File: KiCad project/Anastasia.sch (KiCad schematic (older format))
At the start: 12 parts, among them U1 EFM32GG332

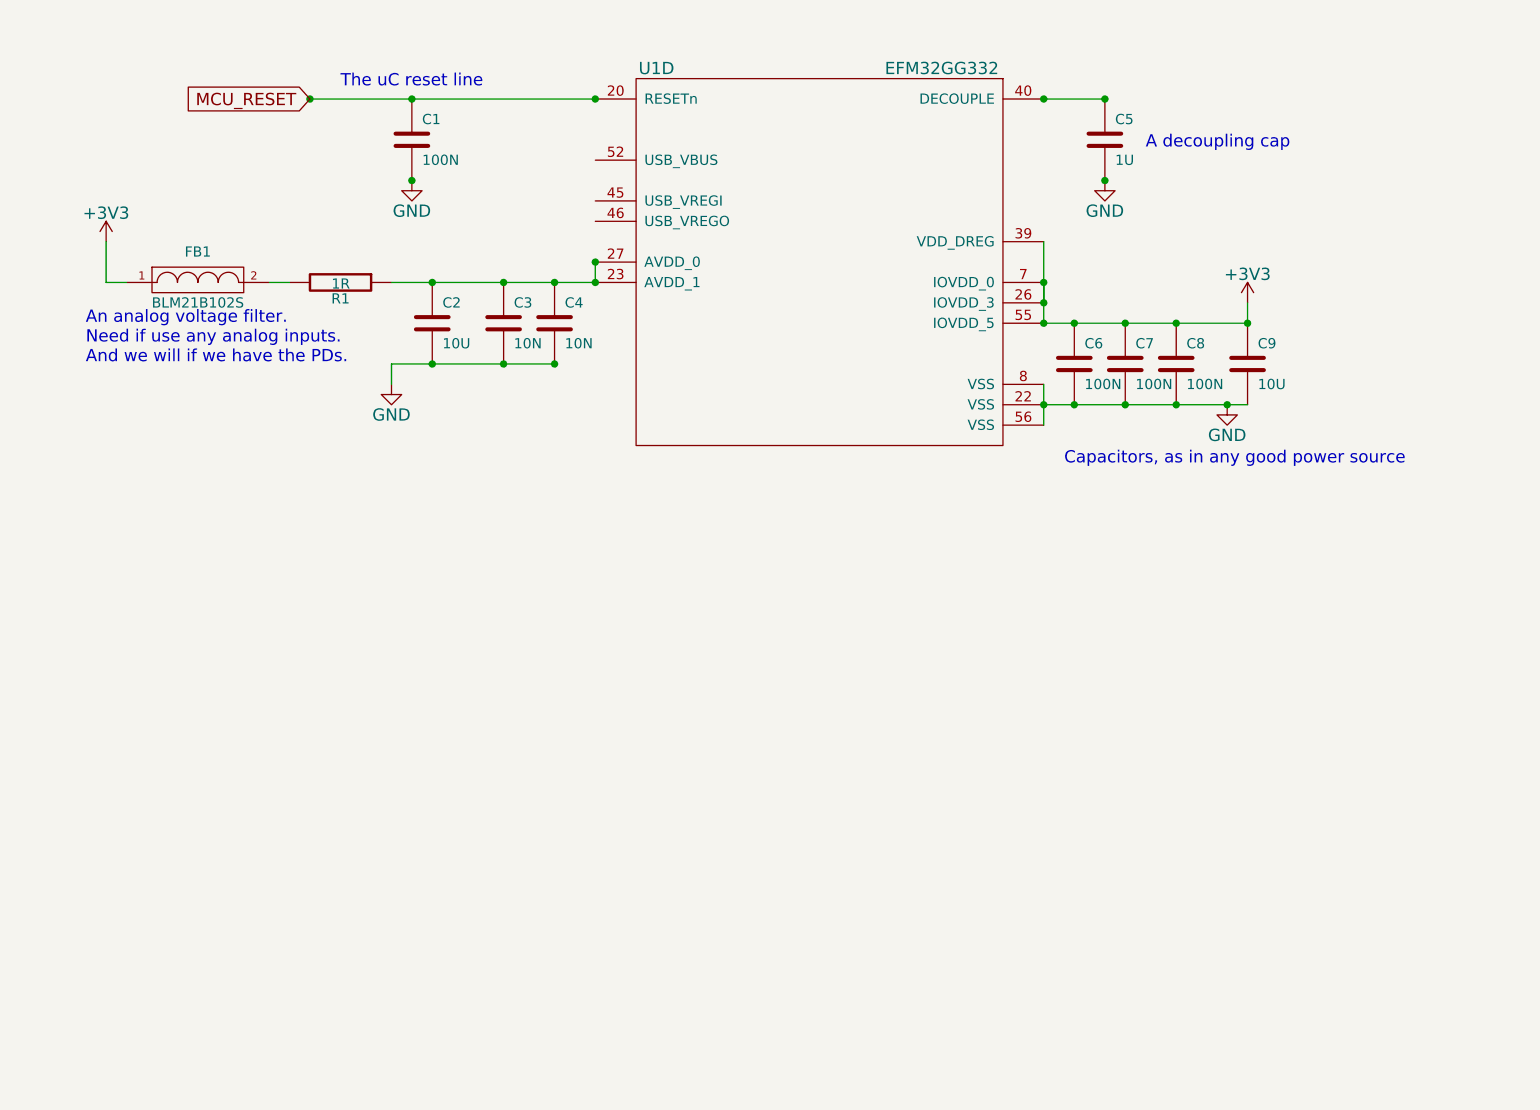
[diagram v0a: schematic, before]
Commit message: Power and USB schematics
The actual schematics file updates
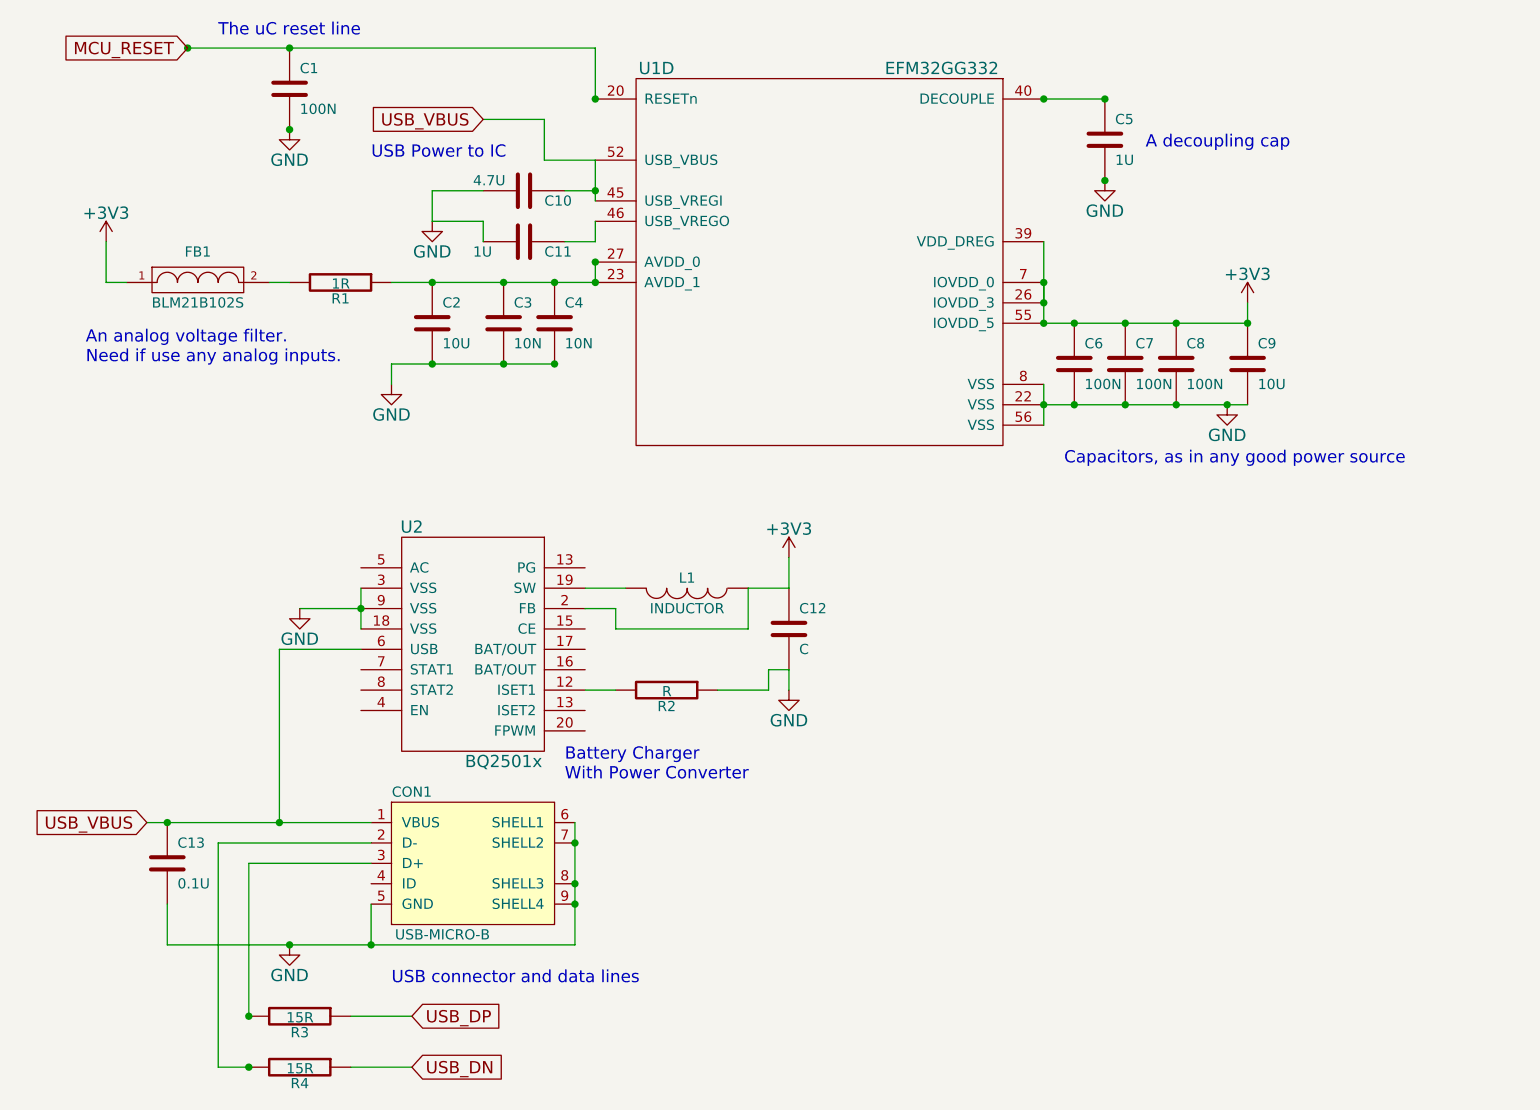
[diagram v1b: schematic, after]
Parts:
- added C10: 4.7U, symbol C
- added C11: 1U, symbol C
- added C12: C, symbol C
- added C13: 0.1U, symbol C
- added CON1: USB-MICRO-B, symbol USB-MICRO-B
- added L1: INDUCTOR, symbol INDUCTOR
- added R2: R, symbol R
- added R3, R4: 15R, symbol R
- added U2: BQ2501x, symbol BQ2501x
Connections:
- net +3V3: now also C12.1, L1.1, U2.2 (FB)
- net GND: now also C10.2, C11.2, C12.2, C13.2, CON1.5 (GND), CON1.6 (SHELL1), CON1.7 (SHELL2), CON1.8 (SHELL3), CON1.9 (SHELL4), R2.1, U2.18 (VSS), U2.3 (VSS), U2.9 (VSS)
- net USB_VBUS: now reaches U1.45 (USB_VREGI)
- net USB_VBUS: now also U1.52 (USB_VBUS), C10.1, C13.1, CON1.1 (VBUS), U2.6 (USB)
- net at U1.46 (USB_VREGO): now also C11.1
- new net: R2.2, U2.12 (ISET1)
- new net: L1.2, U2.19 (SW)
- new net: CON1.2 (D-), R4.2
- new net: CON1.3 (D+), R3.2
- new net USB_DN: R4.1
- new net USB_DP: R3.1
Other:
- note added: "An analog voltage filter. \nNeed if use any analog inputs.\n\n"
- note added: "Battery Charger\nWith Power Converter"
- note added: "USB Power to IC"
- note added: "USB connector and data lines\n"
- note removed: "An analog voltage filter. \nNeed if use any analog inputs.\nAnd we will if we have the PDs.\n\n"
- moved on the sheet: C1

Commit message: IMU and crystal schematics
Added schematics for crystal oscillators of the main uC and schematic
for MPU-9150 and passive components. Miscellaneous updates and
annotations
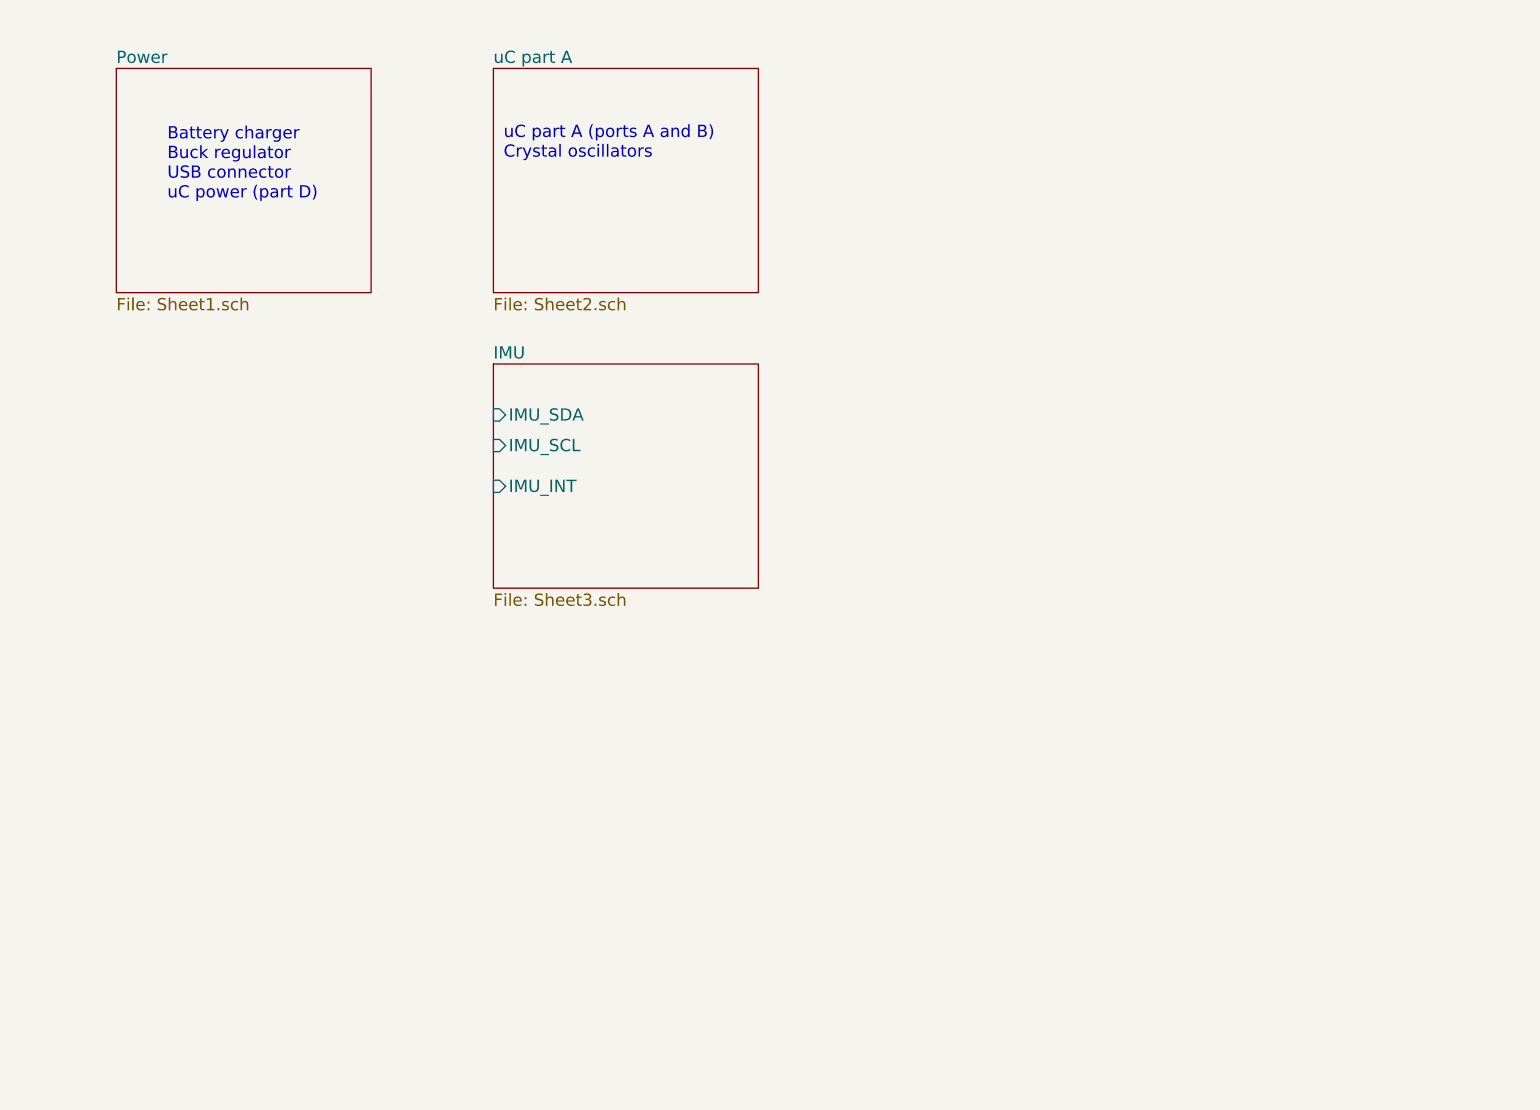
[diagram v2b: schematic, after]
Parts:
- removed C1, C6, C7, C8: 100N, symbol C
- removed C10: 4.7U, symbol C
- removed C11, C5: 1U, symbol C
- removed C12: C, symbol C
- removed C13: 0.1U, symbol C
- removed C2, C9: 10U, symbol C
- removed C3, C4: 10N, symbol C
- removed CON1: USB-MICRO-B, symbol USB-MICRO-B
- removed FB1: BLM21B102S, symbol FILTER
- removed L1: INDUCTOR, symbol INDUCTOR
- removed R1: 1R, symbol R
- removed R2: R, symbol R
- removed R3, R4: 15R, symbol R
- removed U1: EFM32GG332, symbol EFM32GG332
- removed U2: BQ2501x, symbol BQ2501x
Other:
- note added: "Battery charger\nBuck regulator\nUSB connector\nuC power (part D)"
- note added: "uC part A (ports A and B)\nCrystal oscillators\n"
- note removed: "A decoupling cap\n"
- note removed: "An analog voltage filter. \nNeed if use any analog inputs.\n\n"
- note removed: "Battery Charger\nWith Power Converter"
- note removed: "Capacitors, as in any good power source"
- note removed: "The uC reset line"
- note removed: "USB Power to IC"
- note removed: "USB connector and data lines\n"

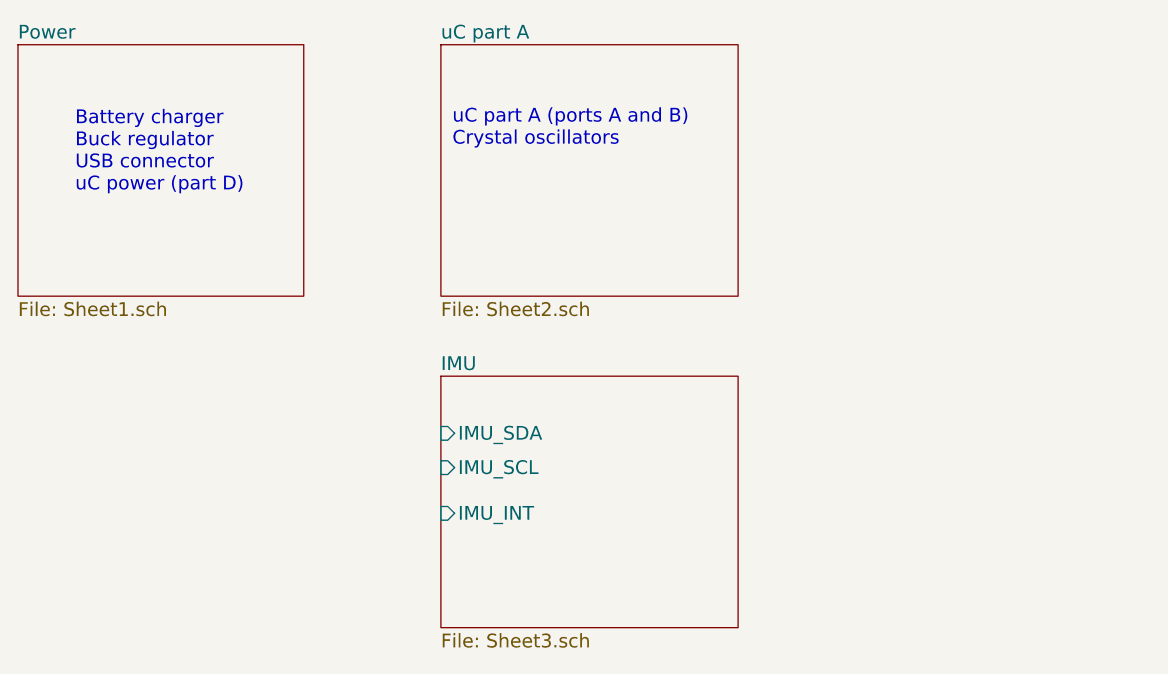
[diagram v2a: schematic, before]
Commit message: Bluetooth schematics
nRF8001 schematics, various additions and modification, test points
added
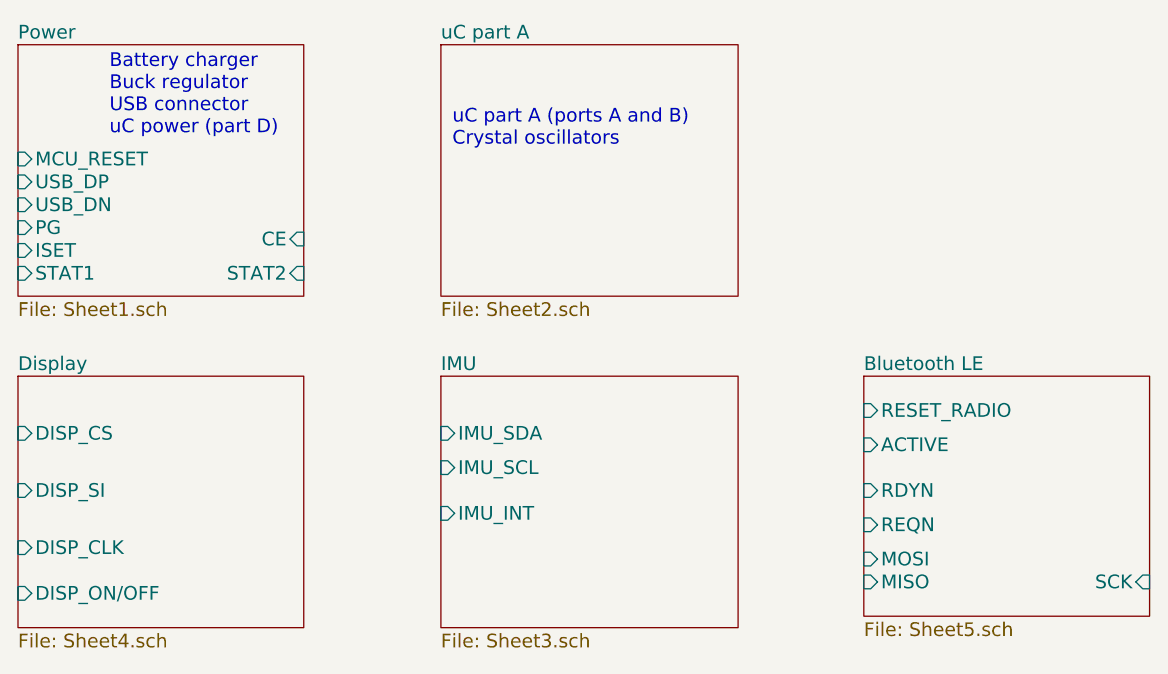
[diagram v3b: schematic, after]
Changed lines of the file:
@@
 $Descr A4 11693 8268
 encoding utf-8
-Sheet 1 4
+Sheet 1 6
 Title "Smartwatch"
 Date "14 March 2015"
@@
 F0 "Power" 60
 F1 "Sheet1.sch" 60
+F2 "MCU_RESET" I L 1100 1350 60
+F3 "USB_DP" I L 1100 1450 60
+F4 "USB_DN" I L 1100 1550 60
+F5 "PG" I L 1100 1650 60
+F6 "ISET" I L 1100 1750 60
+F7 "STAT1" I L 1100 1850 60
+F8 "STAT2" I R 2350 1850 60
+F9 "CE" I R 2350 1700 60
 $EndSheet
-Text Notes 1350 1500 0    60   ~ 0
+Text Notes 1500 1250 0    60   ~ 0
 Battery charger\nBuck regulator\nUSB connector\nuC power (part D)
 $Sheet
@@
 F4 "IMU_INT" I L 2950 2900 60
 $EndSheet
+$Sheet
+S 1100 2300 1250 1100
+U 55054148
+F0 "Display" 60
+F1 "Sheet4.sch" 60
+F2 "DISP_CS" I L 1100 2550 60
+F3 "DISP_SI" I L 1100 2800 60
+F4 "DISP_CLK" I L 1100 3050 60
+F5 "DISP_ON/OFF" I L 1100 3250 60
+$EndSheet
+$Sheet
+S 4800 2300 1250 1050
+U 550556D4
+F0 "Bluetooth LE" 60
+F1 "Sheet5.sch" 60
+F2 "RESET_RADIO" I L 4800 2450 60
+F3 "ACTIVE" I L 4800 2600 60
+F4 "RDYN" I L 4800 2800 60
+F5 "REQN" I L 4800 2950 60
+F6 "MOSI" I L 4800 3100 60
+F7 "MISO" I L 4800 3200 60
+F8 "SCK" I R 6050 3200 60
+$EndSheet
 $EndSCHEMATC
